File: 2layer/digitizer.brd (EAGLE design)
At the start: 76.2 x 51.3 mm, 60 parts, among them IC1 FT601QQFN76, X1 SMA-142-0711-881/886, X2 SMA-142-0711-881/886

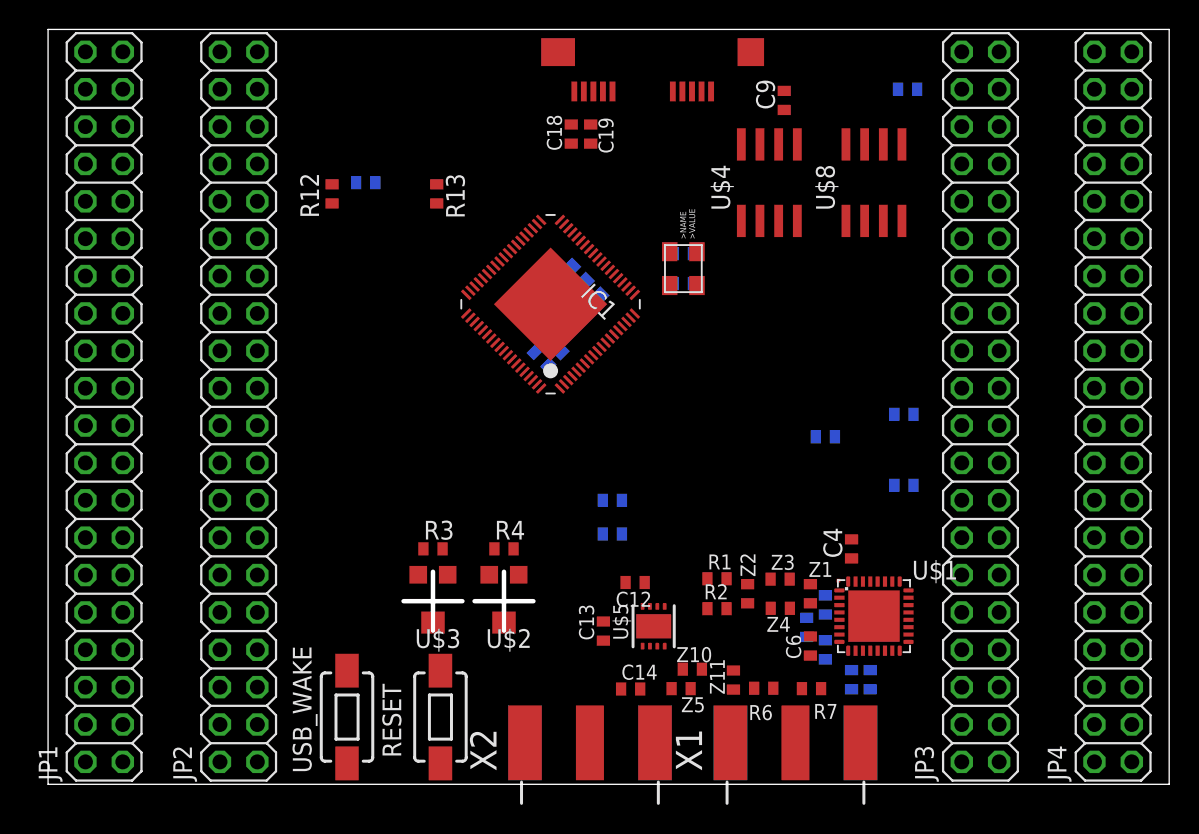
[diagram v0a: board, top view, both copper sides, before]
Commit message: added pours
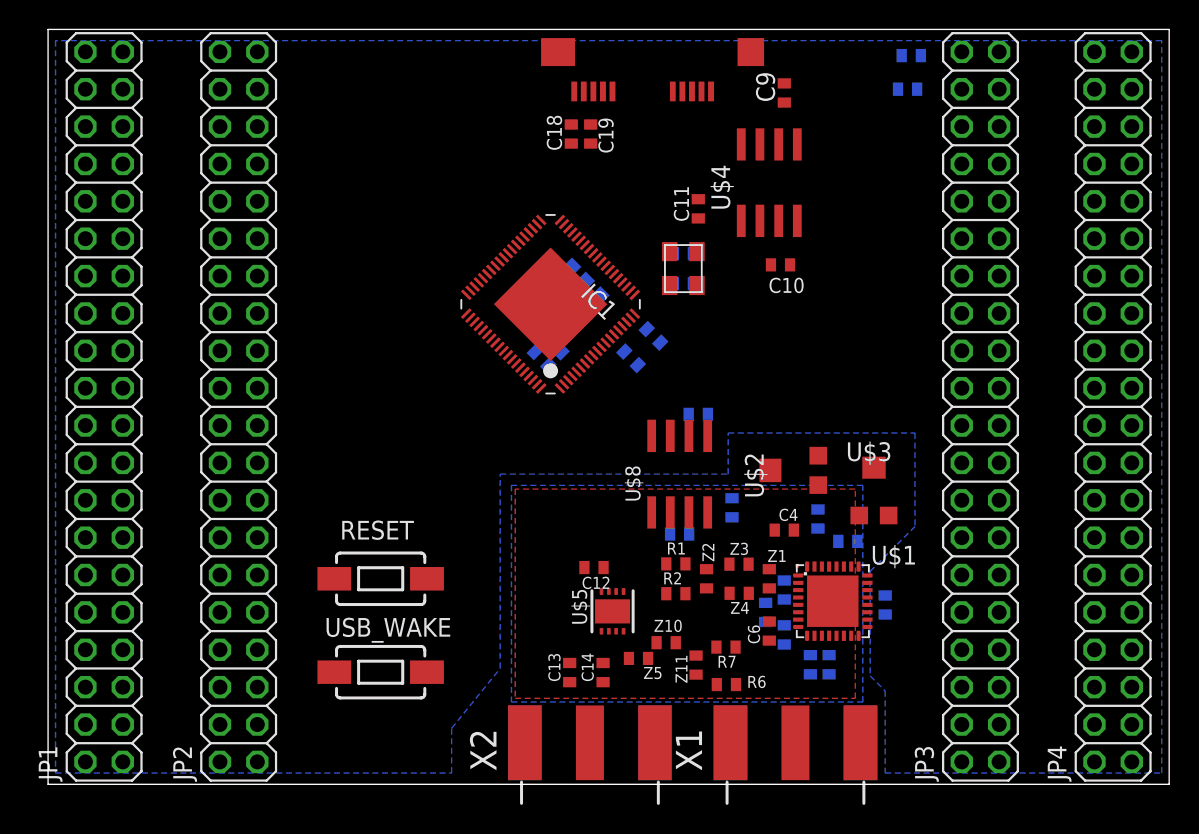
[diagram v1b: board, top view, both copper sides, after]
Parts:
- U$4, U$8: value LT1763CS8-3 -> LT1763CS8-3.3
- moved R17 38.1 mm to (58.7, 49.5)
- moved U$3 30.9 mm to (56.1, 20.1), turned to 0 degrees
- moved R3 28.2 mm to (54.4, 16.5), flipped to the bottom, turned to 180 degrees
- moved U$8 23.8 mm to (42.9, 21.1)
- moved R12 23.2 mm to (39.6, 29.0), flipped to the bottom, turned to 45 degrees
- moved C10 21.6 mm to (49.8, 35.3), flipped to the top, turned to 0 degrees
- moved U$2 21.5 mm to (50.5, 21.3), turned to 90 degrees
- moved R4 21.4 mm to (52.3, 18.0), flipped to the bottom, turned to 90 degrees
- moved C11 20.7 mm to (44.2, 39.1), flipped to the top, turned to 270 degrees
- moved R13 17.6 mm to (41.1, 30.5), flipped to the bottom, turned to 45 degrees
- moved C25 15.6 mm to (42.9, 17.0), turned to 180 degrees
- moved C24 13.3 mm to (46.5, 18.8), turned to 270 degrees
- moved RESET 10.2 mm to (22.6, 14.0), turned to 0 degrees
- moved C23 8.77 mm to (44.2, 25.1)
- moved R7 6.46 mm to (46.1, 9.32)
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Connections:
- new net AGND: C1.2, C12.2, C2.2, C25.2, C4.2, C7.2, C8.2, R3.1, R4.1, U$1.8, U$1.EXP, U$5.EXP, U$8.3
- net AVDD: no longer R12.1, R13.1
- net DVDD: now also R12.1, R13.1
- net GND: no longer C1.2, C12.2, C2.2, C25.2, C4.2, C7.2, C8.2, R3.1, R4.1, U$1.8, U$1.EXP, U$5.EXP, U$8.3
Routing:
- added copper zone on layer 1, net AGND
- added copper zone on layer 16, net AGND
- added copper zone on layer 16, net GND

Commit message: autorouter sucks, trying manual
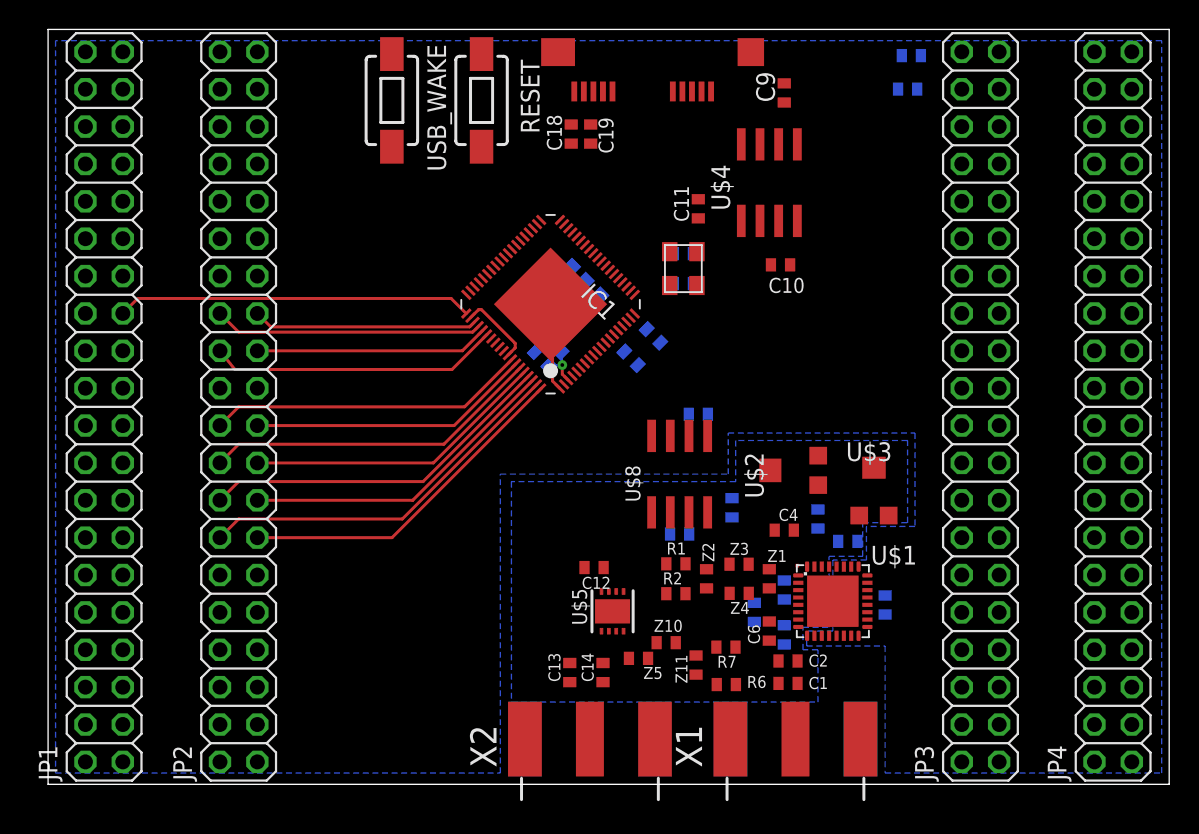
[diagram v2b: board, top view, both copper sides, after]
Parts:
- moved USB_WAKE 38.9 mm to (23.4, 46.5), turned to 270 degrees
- moved RESET 33.2 mm to (29.5, 46.5), turned to 270 degrees
- moved C2 2.81 mm to (50.3, 8.38), flipped to the top, turned to 180 degrees
- moved C1 1.98 mm to (50.3, 6.86), flipped to the top, turned to 180 degrees
- moved C5 0.76 mm to (48.0, 11.7)
- moved X1 0.25 mm to (50.8, 0.51)
- moved X2 0.25 mm to (36.8, 0.51)
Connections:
- net UDAT16: now also JP2.25; no longer JP2.26
- net UDAT17: now also JP2.26; no longer JP2.25
- net UDAT18: now also JP2.23; no longer JP2.24
- net UDAT19: now also JP2.24; no longer JP2.23
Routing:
- net UDAT30: track 0.00 -> 25.9 mm
- net UDAT28: track 0.00 -> 24.5 mm
- net FCLK: track 0.00 -> 24.2 mm
- net UDAT31: track 0.00 -> 23.5 mm
- net UDAT26: track 0.00 -> 23.1 mm
- net UDAT29: track 0.00 -> 22.1 mm
- net UDAT24: track 0.00 -> 21.7 mm
- net UDAT27: track 0.00 -> 20.7 mm
- net UDAT19: track 0.00 -> 19.8 mm
- net UDAT25: track 0.00 -> 19.3 mm
- net UDAT17: track 0.00 -> 18.3 mm
- net UDAT18: track 0.00 -> 15.9 mm
- net UDAT16: track 0.00 -> 15.3 mm
- net DVDD: track 0.00 -> 5.23 mm
- net V1REF: track 0.00 -> 3.05 mm, vias 0 -> 1
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- removed copper zone on layer 1, net AGND

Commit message: routing routing routing....
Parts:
- moved USB_WAKE 36.6 mm to (55.6, 29.2), turned to 0 degrees
- moved R17 24.5 mm to (67.6, 26.7), turned to 270 degrees
- moved RESET 24.2 mm to (46.5, 29.2), turned to 180 degrees
- moved R16 19.5 mm to (67.6, 30.0), turned to 90 degrees
- moved U$8 13.5 mm to (56.4, 22.1)
- moved C25 13.5 mm to (56.4, 17.5), flipped to the top, turned to 0 degrees
- moved C23 11.3 mm to (55.1, 27.9), turned to 180 degrees
- moved C24 10.5 mm to (56.4, 15.2), flipped to the top, turned to 0 degrees
- moved R10 9.95 mm to (39.6, 42.5), flipped to the top, turned to 270 degrees
- moved R4 8.92 mm to (43.4, 17.3), flipped to the top
- moved Z2 6.60 mm to (38.2, 14.0)
- moved C14 6.60 mm to (31.1, 7.59)
- moved C12 6.60 mm to (30.5, 14.7)
- moved C13 6.60 mm to (28.9, 7.59)
- moved R1 6.60 mm to (36.1, 15.0)
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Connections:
- net SFT_RSTN: now also JP4.20; no longer JP3.40
- net SFT_WKPN: now also JP4.26; no longer JP3.38
- net UDAT19: no longer JP1.24
- net UDAT21: now also JP1.20
- net UDAT23: now also JP1.17; no longer JP1.20
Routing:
- net DVDD: track 5.23 -> 48.5 mm, vias 0 -> 4
- net AVDD: track 0.00 -> 41.7 mm, vias 0 -> 3
- net UDAT21: track 0.00 -> 30.2 mm, vias 0 -> 1
- net UDAT23: track 0.00 -> 29.0 mm, vias 0 -> 1
- net GPIO0: track 0.00 -> 28.9 mm
- net GND: track 2.26 -> 30.6 mm, vias 0 -> 31
- net UDAT11: track 0.00 -> 28.1 mm
- net UDAT22: track 0.00 -> 27.8 mm, vias 0 -> 1
- net UDAT10: track 0.00 -> 26.8 mm, vias 0 -> 1
- net UDAT20: track 0.00 -> 26.6 mm, vias 0 -> 1
- net UDAT15: track 0.00 -> 26.4 mm, vias 0 -> 1
- net UDAT1: track 0.00 -> 26.2 mm
- net GPIO1: track 0.00 -> 25.1 mm
- net UDAT3: track 0.00 -> 24.9 mm
- net UDAT14: track 0.00 -> 24.5 mm
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- added copper zone on layer 1, net DVDD
- added copper zone on layer 16, net DVDD
- added copper zone on layer 1, net GND
- added copper zone on layer 16, net LO-
- added copper zone on layer 16, net N$1
- added copper zone on layer 1, net VBUS
